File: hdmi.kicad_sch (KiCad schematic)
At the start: 11 parts, among them J15 Rasp_HDMI, J16 HDMI_OUT, U10 TS3DV642A0RUAR, U9 LM1117DT-3.3

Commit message: fix hdmi traces and push button kill pin supply
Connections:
- net CK+A renamed CKA+
- net CK+B renamed CKB+
- net CK-A renamed CKA-
- net CK-B renamed CKB-
- net D0+A renamed D0A+
- net D0+B renamed D0B+
- net D0-A renamed D0A-
- net D0-B renamed D0B-
- net D1+A renamed D1A+
- net D1+B renamed D1B+
- net D1-A renamed D1A-
- net D1-B renamed D1B-
- net D2+A renamed D2A+
- net D2+B renamed D2B+
- net D2-A renamed D2A-
- net D2-B renamed D2B-
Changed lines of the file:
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@@
 		)
 	)
-	(label "D2+B"
+	(label "D2B+"
 		(at 165.1 93.98 0)
 		(fields_autoplaced yes)
@@
 		)
 	)
-	(label "CK-B"
+	(label "CKB-"
 		(at 165.1 111.76 0)
 		(fields_autoplaced yes)
@@
 		)
 	)
-	(label "D0-B"
+	(label "D0B-"
 		(at 165.1 106.68 0)
 		(fields_autoplaced yes)
@@
 		)
 	)
-	(label "CK+B"
+	(label "CKB+"
 		(at 165.1 109.22 0)
 		(fields_autoplaced yes)
@@
 		)
 	)
-	(label "D1-B"
+	(label "D1B-"
 		(at 165.1 101.6 0)
 		(fields_autoplaced yes)
@@
 		)
 	)
-	(label "D1+B"
+	(label "D1B+"
 		(at 165.1 99.06 0)
 		(fields_autoplaced yes)
@@
 		)
 	)
-	(label "D0+B"
+	(label "D0B+"
 		(at 165.1 104.14 0)
 		(fields_autoplaced yes)
@@
 		)
 	)
-	(label "D2-B"
+	(label "D2B-"
 		(at 165.1 96.52 0)
 		(fields_autoplaced yes)
@@
 		)
 	)
-	(global_label "D2+A"
+	(global_label "D2A+"
 		(shape input)
 		(at 169.545 55.88 0)
@@
 		)
 	)
-	(global_label "CK-A"
+	(global_label "CKA-"
 		(shape input)
 		(at 169.545 73.66 0)
@@
 		)
 	)
-	(global_label "D1-A"
+	(global_label "D1A-"
 		(shape input)
 		(at 169.545 63.5 0)
@@
 		)
 	)
-	(global_label "D1+A"
+	(global_label "D1A+"
 		(shape input)
 		(at 169.545 60.96 0)
@@
 		)
 	)
-	(global_label "D0-A"
+	(global_label "D0A-"
 		(shape input)
 		(at 169.545 68.58 0)
@@
 		)
 	)
-	(global_label "CK+A"
+	(global_label "CKA+"
 		(shape input)
 		(at 169.545 71.12 0)
@@
 		)
 	)
-	(global_label "D0+A"
+	(global_label "D0A+"
 		(shape input)
 		(at 169.545 66.04 0)
@@
 		)
 	)
-	(global_label "D2-A"
+	(global_label "D2A-"
 		(shape input)
 		(at 169.545 58.42 0)

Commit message: update layout pcb & zip tesi
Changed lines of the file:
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@@
 	(wire
 		(pts
-			(xy 183.515 88.9) (xy 183.515 116.84)
+			(xy 184.15 88.9) (xy 184.15 116.84)
 		)
 		(stroke
@@
 	(wire
 		(pts
-			(xy 183.515 116.84) (xy 189.23 116.84)
+			(xy 184.15 116.84) (xy 189.23 116.84)
 		)
 		(stroke
@@
 	(wire
 		(pts
-			(xy 155.575 88.9) (xy 183.515 88.9)
-		)
-		(stroke
+			(xy 155.575 88.9) (xy 184.15 88.9)
+		)
+		(stroke

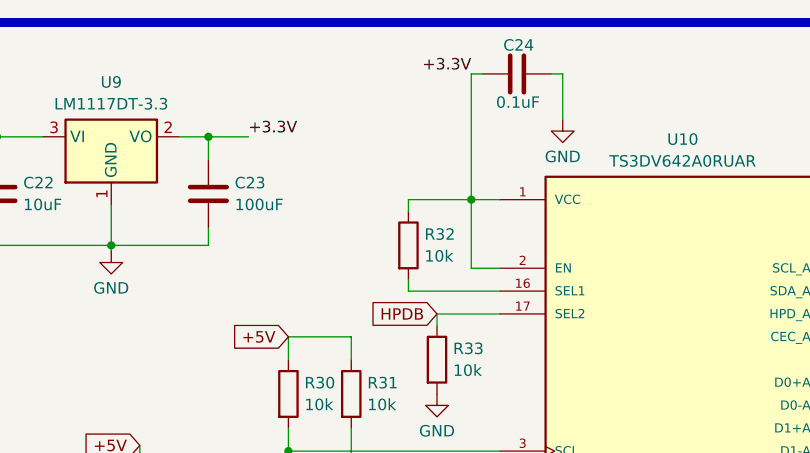
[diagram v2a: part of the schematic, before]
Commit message: aggiunto pin enable switch per schermo composito
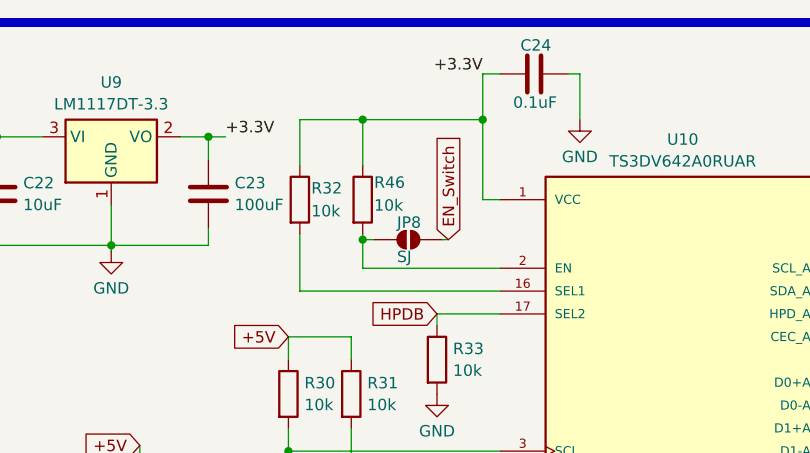
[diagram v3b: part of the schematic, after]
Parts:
- added JP8: SJ, Jumper:SolderJumper-2_P1.3mm_Open_Pad1.0x1.5mm, symbol Jumper:SolderJumper_2_Open
- added R46: 10k, Resistor_SMD:R_0603_1608Metric_Pad0.98x0.95mm_HandSolder, symbol Device:R
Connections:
- net +3.3V: now also R46.1; no longer U10.2 (EN)
- new net: JP8.2 (B), R46.2, U10.2 (EN)
- new net EN_Switch: JP8.1 (A)
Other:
- moved on the sheet: C24, R32

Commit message: update zip
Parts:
- C23: footprint Capacitor_SMD:C_0603_1608Metric_Pad1.08x0.95mm_HandSolder -> Capacitor_SMD:C_1206_3216Metric_Pad1.33x1.80mm_HandSolder
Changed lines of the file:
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@@
 			)
 		)
-		(property "Footprint" "Capacitor_SMD:C_0603_1608Metric_Pad1.08x0.95mm_HandSolder"
+		(property "Footprint" "Capacitor_SMD:C_1206_3216Metric_Pad1.33x1.80mm_HandSolder"
 			(at 83.5152 38.735 0)
 			(effects
